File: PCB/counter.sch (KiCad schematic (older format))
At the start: 17 parts, among them P1 9V, Q1 2N3904, SW1 ПАУЗА, SW2 СБРОС, U1 4050, U2 LM7805, U3 ArduinoNano, U4 4_Digit_Display_Board, U5 Hall_Sensor

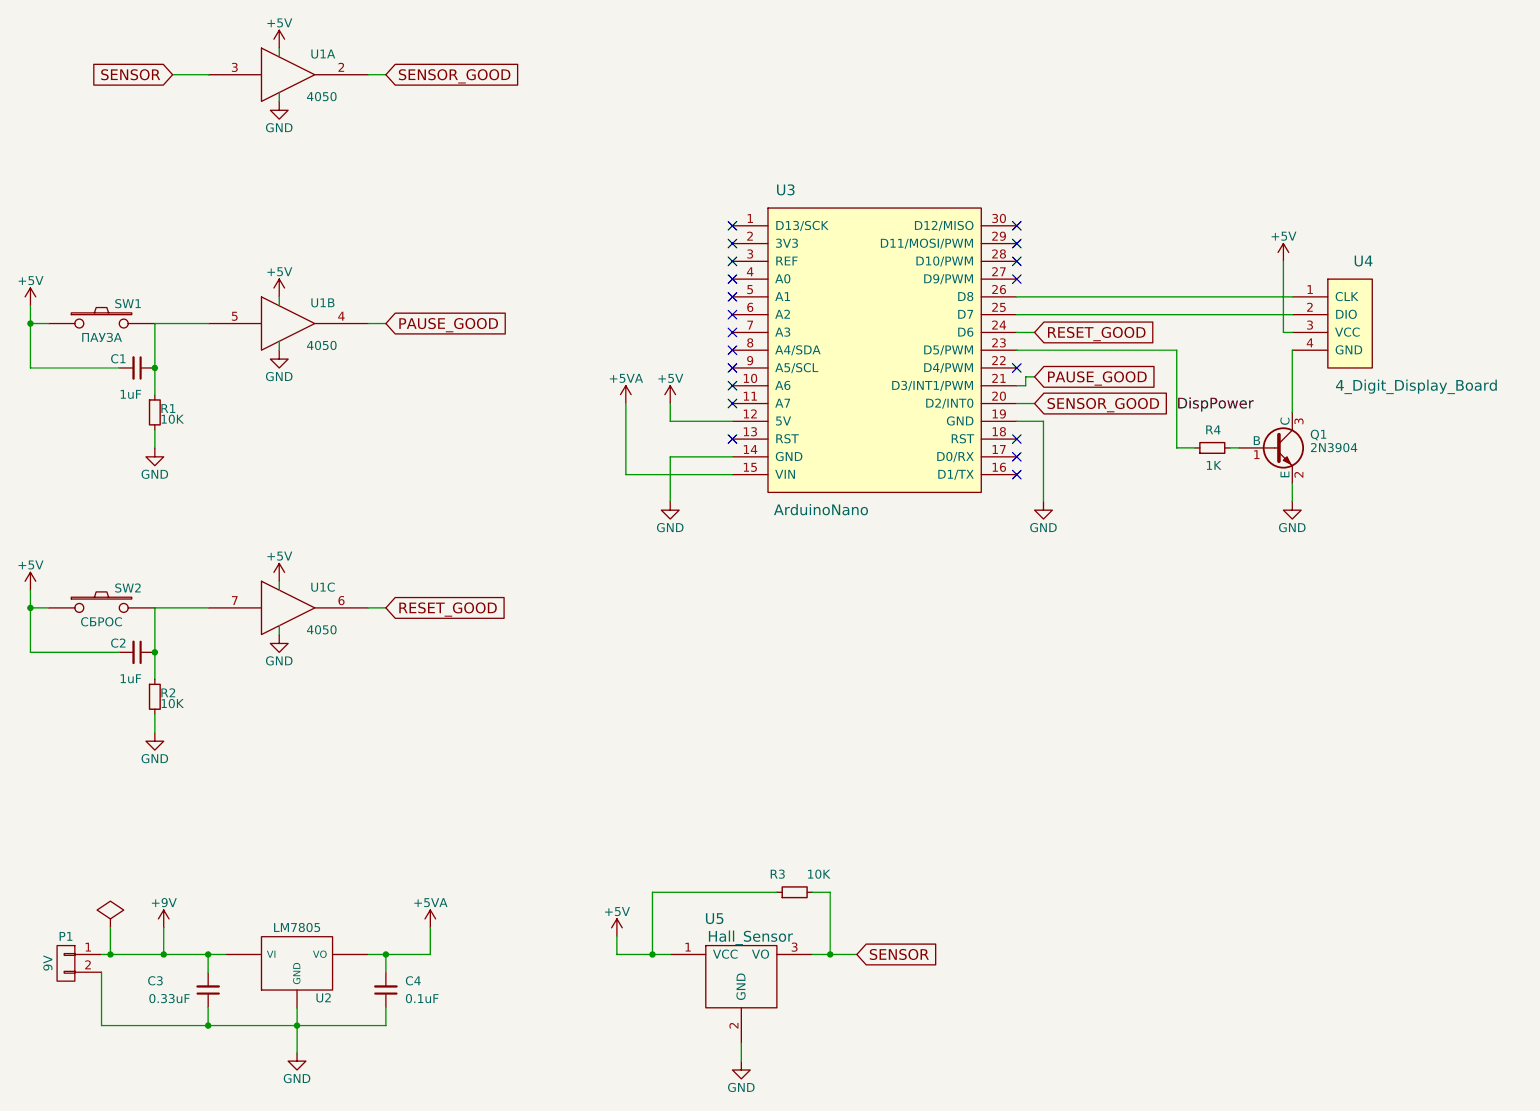
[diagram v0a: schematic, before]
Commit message: Первое приближение разводки Добавил выключатель с фиксатором на батарейку
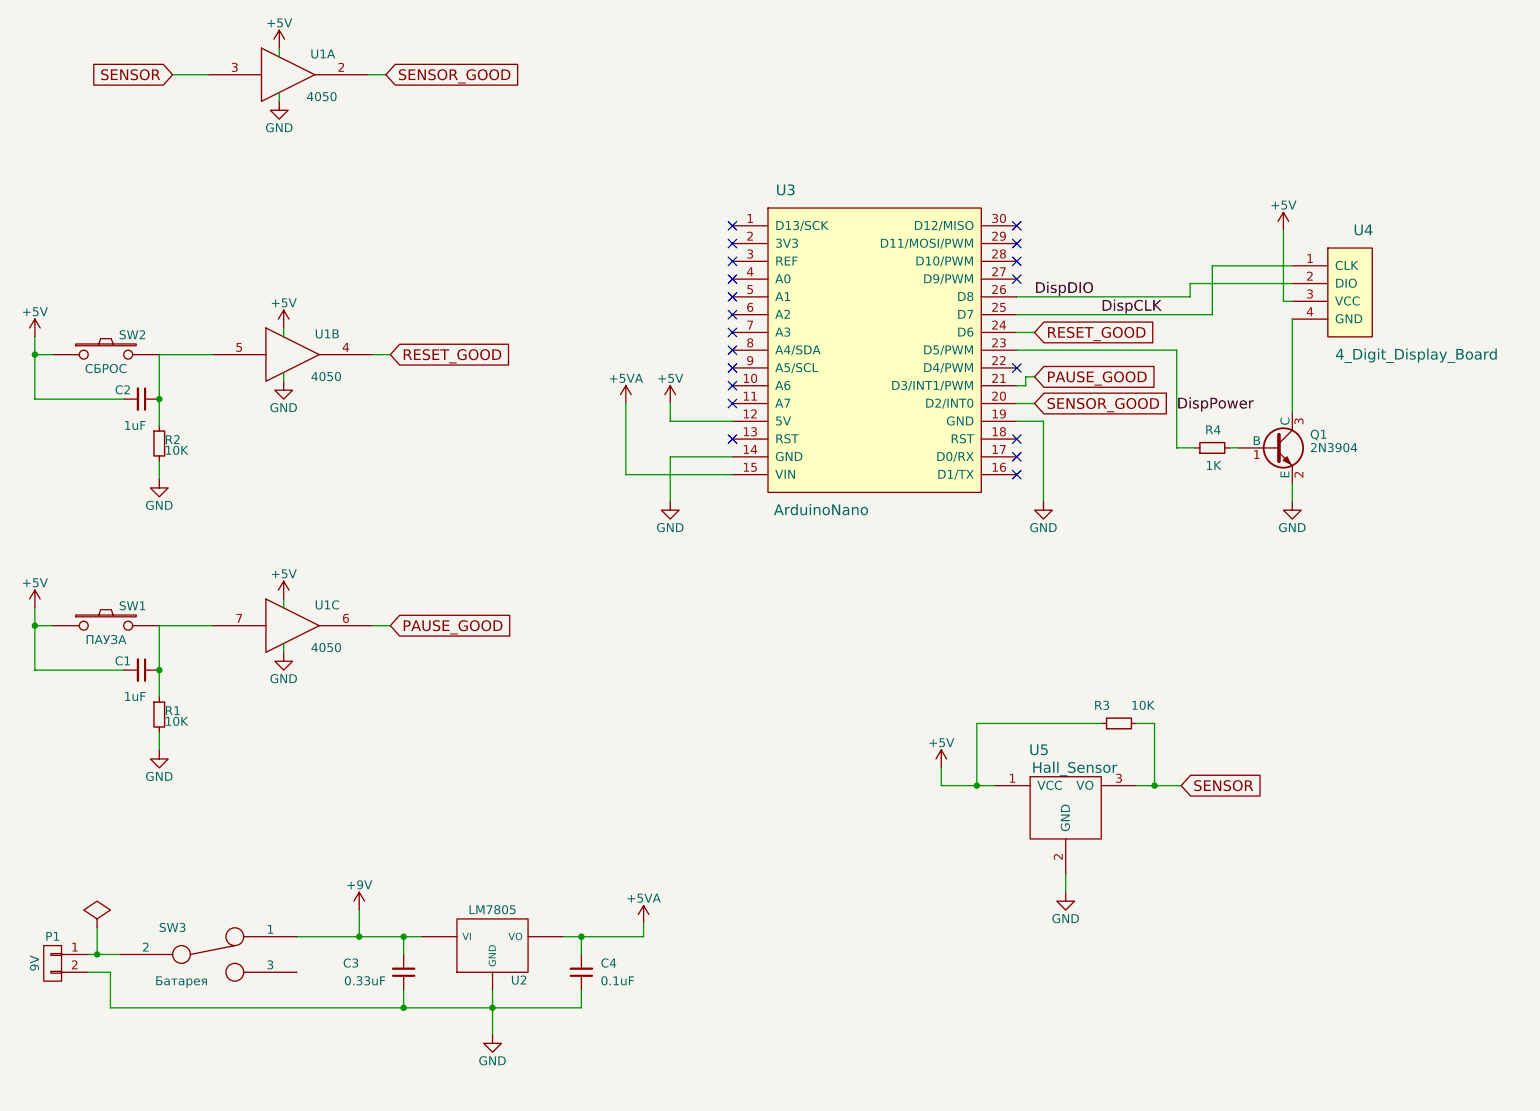
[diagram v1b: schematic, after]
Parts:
- added SW3: Батарея, Buttons_Switches_ThroughHole:SW_PUSH_x2, symbol SWITCH_INV
- U2: footprint TO_SOT_Packages_THT:TO-220_Neutral123_Horizontal_LargePads -> Libraries:LM7805_TO-220_Neutral123_Horizontal_LargePads_with_GND_pad
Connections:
- net +9V: now also SW3.1; no longer P1.1 (P1)
- net PAUSE_GOOD: now also U1.6; no longer U1.4
- net RESET_GOOD: now also U1.4; no longer U1.6
- net DispCLK: now reaches U3.25 (D7)
- net DispCLK: now also U4.1 (CLK); no longer U4.2 (DIO)
- net DispDIO: now reaches U3.26 (D8)
- net DispDIO: now also U4.2 (DIO); no longer U4.1 (CLK)
- net at C1.1, R1.1, SW1.2: now also U1.7; no longer U1.5
- net at C2.1, R2.1, SW2.2: now also U1.5; no longer U1.7
- new net: P1.1 (P1), SW3.2
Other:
- moved on the sheet: C1, C2, C3, C4, P1, R1, R2, R3, SW1, SW2, U2, U4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

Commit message: Добавил инкрементальную кнопку
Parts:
- added SW4: +1, Libraries:Btn_Tack_5mm, symbol SW_PUSH
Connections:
- net GND: now also SW4.2
- net SENSOR: now also SW4.1
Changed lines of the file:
@@
 $EndComp
 $Comp
-L +5V #PWR01
+L +5V #PWR20
 U 1 1 56E7DD8C
 P 8100 2125
-F 0 "#PWR01" H 8100 1975 50  0001 C CNN
+F 0 "#PWR20" H 8100 1975 50  0001 C CNN
 F 1 "+5V" H 8100 2265 50  0000 C CNN
 F 2 "" H 8100 2125 50  0000 C CNN
@@
 	8100 2525 8150 2525
 $Comp
-L GND #PWR02
+L GND #PWR18
 U 1 1 56E7DDB2
 P 6750 3650
-F 0 "#PWR02" H 6750 3400 50  0001 C CNN
+F 0 "#PWR18" H 6750 3400 50  0001 C CNN
 F 1 "GND" H 6750 3500 50  0000 C CNN
 F 2 "" H 6750 3650 50  0000 C CNN
@@
 $EndComp
 $Comp
-L +5V #PWR03
+L +5V #PWR15
 U 1 1 56E7DDCC
 P 4650 3100
-F 0 "#PWR03" H 4650 2950 50  0001 C CNN
+F 0 "#PWR15" H 4650 2950 50  0001 C CNN
 F 1 "+5V" H 4650 3240 50  0000 C CNN
 F 2 "" H 4650 3100 50  0000 C CNN
@@
 $EndComp
 $Comp
-L GND #PWR04
+L GND #PWR19
 U 1 1 56E7DFFA
 P 6875 5850
-F 0 "#PWR04" H 6875 5600 50  0001 C CNN
+F 0 "#PWR19" H 6875 5600 50  0001 C CNN
 F 1 "GND" H 6875 5700 50  0000 C CNN
 F 2 "" H 6875 5850 50  0000 C CNN
@@
 $EndComp
 $Comp
-L GND #PWR05
+L GND #PWR22
 U 1 1 56E7E02A
 P 8150 3650
-F 0 "#PWR05" H 8150 3400 50  0001 C CNN
+F 0 "#PWR22" H 8150 3400 50  0001 C CNN
 F 1 "GND" H 8150 3500 50  0000 C CNN
 F 2 "" H 8150 3650 50  0000 C CNN
@@
 $EndComp
 $Comp
-L +5V #PWR06
+L +5V #PWR17
 U 1 1 56E7E060
 P 6175 5150
-F 0 "#PWR06" H 6175 5000 50  0001 C CNN
+F 0 "#PWR17" H 6175 5000 50  0001 C CNN
 F 1 "+5V" H 6175 5290 50  0000 C CNN
 F 2 "" H 6175 5150 50  0000 C CNN
@@
 $EndComp
 $Comp
-L +5V #PWR07
+L +5V #PWR5
 U 1 1 56E7ED46
 P 2450 1100
-F 0 "#PWR07" H 2450 950 50  0001 C CNN
+F 0 "#PWR5" H 2450 950 50  0001 C CNN
 F 1 "+5V" H 2450 1240 50  0000 C CNN
 F 2 "" H 2450 1100 50  0000 C CNN
@@
 	2450 1100 2450 1150
 $Comp
-L GND #PWR08
+L GND #PWR6
 U 1 1 56E7ED99
 P 2450 1400
-F 0 "#PWR08" H 2450 1150 50  0001 C CNN
+F 0 "#PWR6" H 2450 1150 50  0001 C CNN
 F 1 "GND" H 2450 1250 50  0000 C CNN
 F 2 "" H 2450 1400 50  0000 C CNN
@@
 Connection ~ 1775 4600
 $Comp
-L +5V #PWR09
+L +5V #PWR2
 U 1 1 56E7FBA0
 P 1075 4250
-F 0 "#PWR09" H 1075 4100 50  0001 C CNN
+F 0 "#PWR2" H 1075 4100 50  0001 C CNN
 F 1 "+5V" H 1075 4390 50  0000 C CNN
 F 2 "" H 1075 4250 50  0000 C CNN
@@
 Connection ~ 1075 4350
 $Comp
-L GND #PWR010
+L GND #PWR4
 U 1 1 56E7FBAA
 P 1775 5050
-F 0 "#PWR010" H 1775 4800 50  0001 C CNN
+F 0 "#PWR4" H 1775 4800 50  0001 C CNN
 F 1 "GND" H 1775 4900 50  0000 C CNN
 F 2 "" H 1775 5050 50  0000 C CNN
@@
 	1775 4350 2075 4350
 $Comp
-L +5V #PWR011
+L +5V #PWR9
 U 1 1 56E7FBB8
 P 2475 4200
-F 0 "#PWR011" H 2475 4050 50  0001 C CNN
+F 0 "#PWR9" H 2475 4050 50  0001 C CNN
 F 1 "+5V" H 2475 4340 50  0000 C CNN
 F 2 "" H 2475 4200 50  0000 C CNN
@@
 	2475 4200 2475 4250
 $Comp
-L GND #PWR012
+L GND #PWR10
 U 1 1 56E7FBBF
 P 2475 4500
-F 0 "#PWR012" H 2475 4250 50  0001 C CNN
+F 0 "#PWR10" H 2475 4250 50  0001 C CNN
 F 1 "GND" H 2475 4350 50  0000 C CNN
 F 2 "" H 2475 4500 50  0000 C CNN
@@
 Connection ~ 1775 3075
 $Comp
-L +5V #PWR013
+L +5V #PWR1
 U 1 1 56E8099D
 P 1075 2725
-F 0 "#PWR013" H 1075 2575 50  0001 C CNN
+F 0 "#PWR1" H 1075 2575 50  0001 C CNN
 F 1 "+5V" H 1075 2865 50  0000 C CNN
 F 2 "" H 1075 2725 50  0000 C CNN
@@
 Connection ~ 1075 2825
 $Comp
-L GND #PWR014
+L GND #PWR3
 U 1 1 56E809A7
 P 1775 3525
-F 0 "#PWR014" H 1775 3275 50  0001 C CNN
+F 0 "#PWR3" H 1775 3275 50  0001 C CNN
 F 1 "GND" H 1775 3375 50  0000 C CNN
 F 2 "" H 1775 3525 50  0000 C CNN
@@
 	1775 2825 2075 2825
 $Comp
-L +5V #PWR015
+L +5V #PWR7
 U 1 1 56E809BA
 P 2475 2675
-F 0 "#PWR015" H 2475 2525 50  0001 C CNN
+F 0 "#PWR7" H 2475 2525 50  0001 C CNN
 F 1 "+5V" H 2475 2815 50  0000 C CNN
 F 2 "" H 2475 2675 50  0000 C CNN
@@
 	2475 2675 2475 2725
 $Comp
-L GND #PWR016
+L GND #PWR8
 U 1 1 56E809C1
 P 2475 2975
-F 0 "#PWR016" H 2475 2725 50  0001 C CNN
+F 0 "#PWR8" H 2475 2725 50  0001 C CNN
 F 1 "GND" H 2475 2825 50  0000 C CNN
 F 2 "" H 2475 2975 50  0000 C CNN
@@
 	4150 6500 4150 6400
 $Comp
-L GND #PWR017
+L GND #PWR12
 U 1 1 56E81A5B
 P 3650 6650
-F 0 "#PWR017" H 3650 6400 50  0001 C CNN
+F 0 "#PWR12" H 3650 6400 50  0001 C CNN
 F 1 "GND" H 3650 6500 50  0000 C CNN
 F 2 "" H 3650 6650 50  0000 C CNN
@@
 Connection ~ 3650 6500
 $Comp
-L +5VA #PWR018
+L +5VA #PWR14
 U 1 1 56E81B2D
 P 4500 6025
-F 0 "#PWR018" H 4500 5875 50  0001 C CNN
+F 0 "#PWR14" H 4500 5875 50  0001 C CNN
 F 1 "+5VA" H 4500 6165 50  0000 C CNN
 F 2 "" H 4500 6025 50  0000 C CNN
@@
 $EndComp
 $Comp
-L +9V #PWR019
+L +9V #PWR11
 U 1 1 56E81B63
 P 2900 5950
-F 0 "#PWR019" H 2900 5800 50  0001 C CNN
+F 0 "#PWR11" H 2900 5800 50  0001 C CNN
 F 1 "+9V" H 2900 6090 50  0000 C CNN
 F 2 "" H 2900 5950 50  0000 C CNN
@@
 Connection ~ 3150 6100
 $Comp
-L GND #PWR020
+L GND #PWR16
 U 1 1 56E8218B
 P 4650 3650
-F 0 "#PWR020" H 4650 3400 50  0001 C CNN
+F 0 "#PWR16" H 4650 3400 50  0001 C CNN
 F 1 "GND" H 4650 3500 50  0000 C CNN
 F 2 "" H 4650 3650 50  0000 C CNN
@@
 $EndComp
 $Comp
-L +5VA #PWR021
+L +5VA #PWR13
 U 1 1 56E822AB
 P 4400 3100
-F 0 "#PWR021" H 4400 2950 50  0001 C CNN
+F 0 "#PWR13" H 4400 2950 50  0001 C CNN
 F 1 "+5VA" H 4400 3240 50  0000 C CNN
 F 2 "" H 4400 3100 50  0000 C CNN
@@
 Connection ~ 3150 6500
 $Comp
-L PWR_FLAG #FLG022
+L PWR_FLAG #FLG1
 U 1 1 56E8280B
 P 1425 6050
-F 0 "#FLG022" H 1425 6145 50  0001 C CNN
+F 0 "#FLG1" H 1425 6145 50  0001 C CNN
 F 1 "PWR_FLAG" H 1425 6230 50  0001 C CNN
 F 2 "" H 1425 6050 50  0000 C CNN
@@
 Connection ~ 6375 5250
 Wire Wire Line
-	7275 4900 7375 4900
-Wire Wire Line
 	7375 4900 7375 5250
 Wire Wire Line
@@
 Text Label 7075 2600 0    60   ~ 0
 DispCLK
+$Comp
+L SW_PUSH SW4
+U 1 1 56EA8CD8
+P 7800 4900
+F 0 "SW4" H 7950 5010 50  0000 C CNN
+F 1 "+1" H 7800 4820 50  0000 C CNN
+F 2 "Libraries:Btn_Tack_5mm" H 7800 4900 50  0001 C CNN
+F 3 "" H 7800 4900 50  0000 C CNN
+F 4 "0" H 7800 4900 60  0001 C CNN "Price"
+F 5 "TNT" H 7800 4900 60  0001 C CNN "Package"
+F 6 "~" H 7800 4900 60  0001 C CNN "Model"
+F 7 "~" H 7800 4900 60  0001 C CNN "Part №"
+F 8 "button" H 7800 4900 60  0001 C CNN "Type"
+	1    7800 4900
+	1    0    0    -1
+$EndComp
+Connection ~ 7375 4900
+Wire Wire Line
+	7275 4900 7500 4900
+$Comp
+L GND #PWR21
+U 1 1 56EA9427
+P 8100 5000
+F 0 "#PWR21" H 8100 4750 50  0001 C CNN
+F 1 "GND" H 8100 4850 50  0000 C CNN
+F 2 "" H 8100 5000 50  0000 C CNN
+F 3 "" H 8100 5000 50  0000 C CNN
+	1    8100 5000
+	1    0    0    -1
+$EndComp
+Wire Wire Line
+	8100 4900 8100 5000
 $EndSCHEMATC
